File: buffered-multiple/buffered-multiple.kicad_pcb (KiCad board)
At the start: 2 copper layers, 129.5 x 128.5 mm, 67 parts, among them J1 AudioJack_Switch, J10 AudioJack_Switch, J11 Conn_01x06_Pin, J12 Conn_01x06_Socket, J13 AudioJack_Switch, J14 AudioJack_Switch, J15 Conn_02x08_Odd_Even, J16 Conn_01x04_Pin, J17 Conn_01x04_Socket, J2 AudioJack_Switch, J3 AudioJack_Switch, J4 AudioJack_Switch, J5 AudioJack_Switch, J6 AudioJack_Switch, J7 Conn_01x06_Socket, J8 Conn_01x06_Pin, J9 AudioJack_Switch, U1 TL074, U2 TL072, U3 TL074

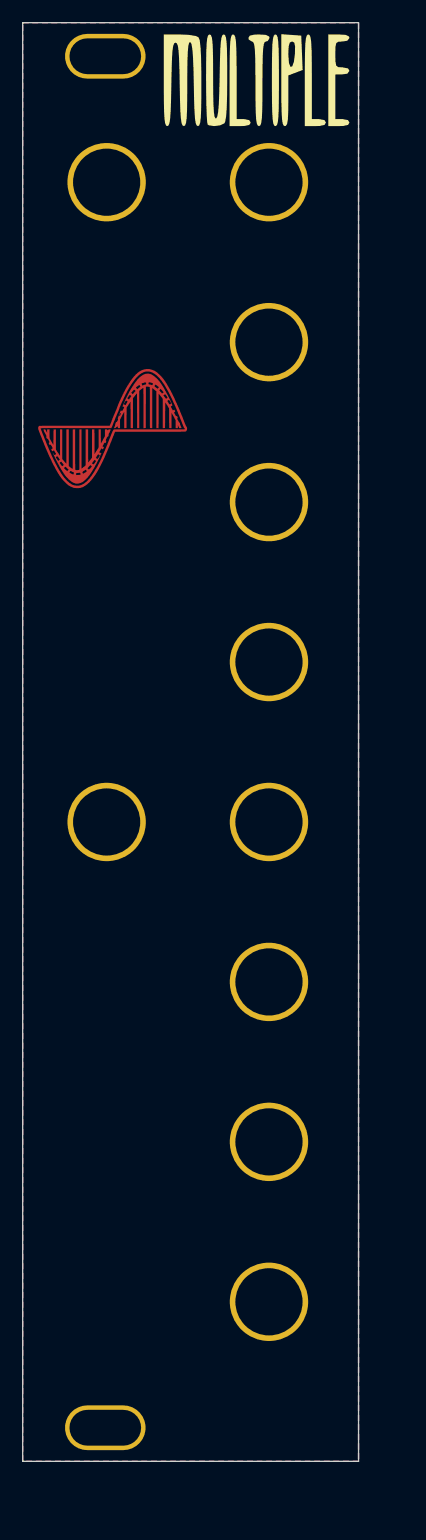
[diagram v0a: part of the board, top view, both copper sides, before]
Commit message: Exponential VCA ver. 1.2
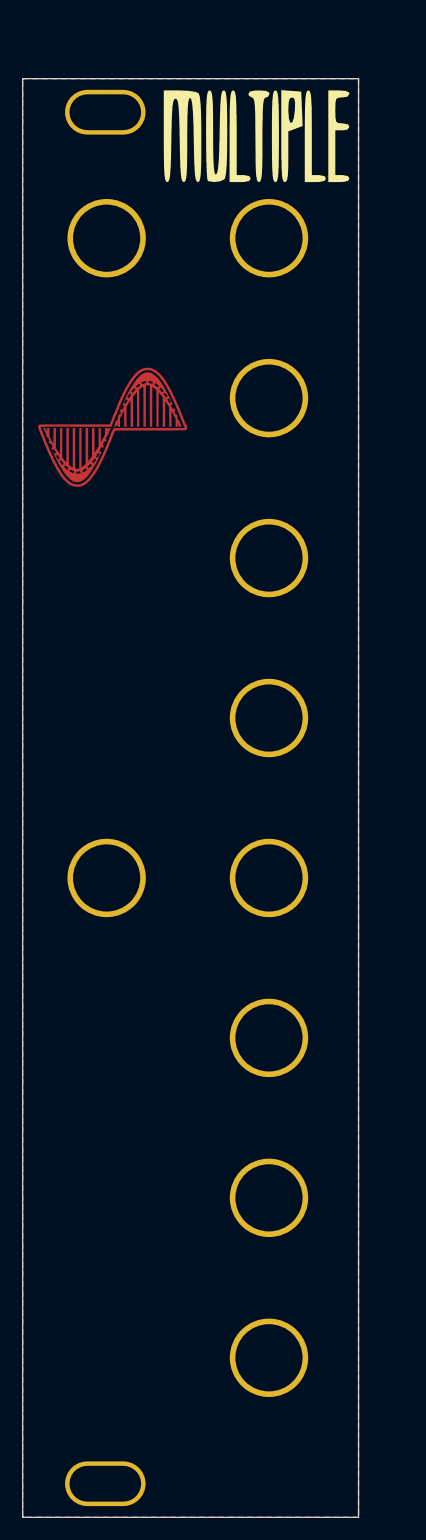
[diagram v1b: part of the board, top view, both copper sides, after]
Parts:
- moved Front 5.00 mm to (39.2, 40.8)
- moved G*** 5.00 mm to (56.0, 46.0)
- moved H3 5.00 mm to (42.5, 55.0)
- moved H8 5.00 mm to (57.0, 55.0)
- moved REF** 5.00 mm to (57.0, 97.9)
- moved REF** 5.00 mm to (42.5, 112.1)
- moved REF** 5.00 mm to (57.0, 126.4)
- moved REF** 5.00 mm to (57.0, 69.3)
- moved REF** 5.00 mm to (50.0, 105.0)
- moved REF** 5.00 mm to (57.0, 155.0)
- moved REF** 5.00 mm to (57.0, 140.7)
- moved REF** 5.00 mm to (57.0, 112.1)
- moved REF** 5.00 mm to (57.0, 83.6)
- moved H1 0.12 mm to (43.0, 71.9)
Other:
- outline, holes or cut-outs redrawn

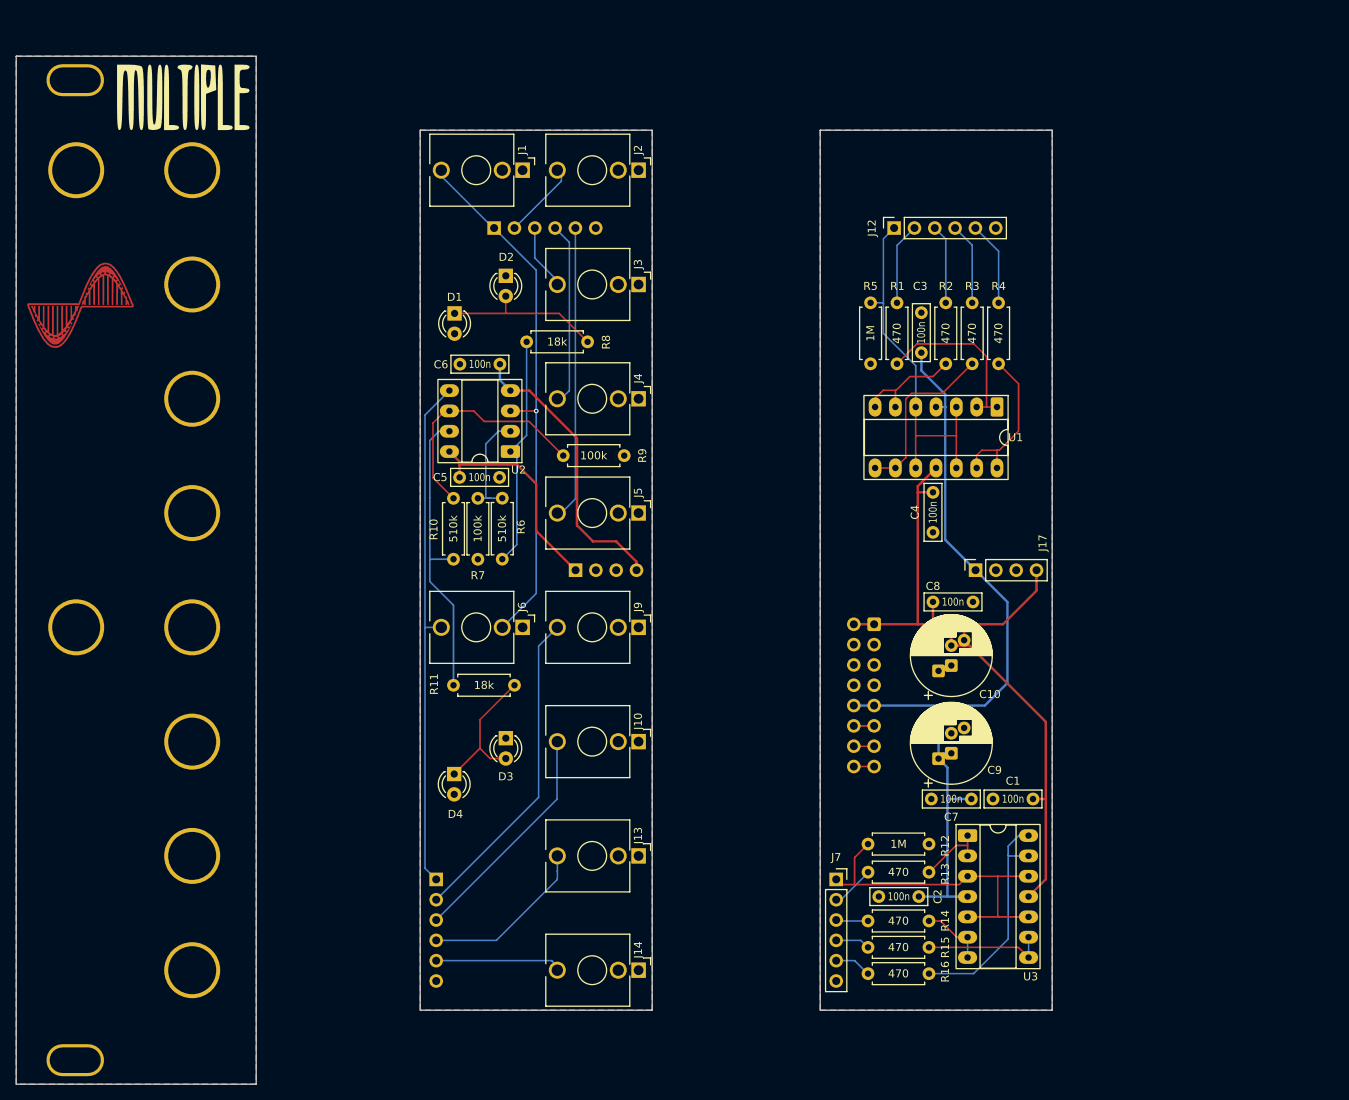
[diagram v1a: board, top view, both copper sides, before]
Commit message: Fixed buffered multiple reversed polarity problem.
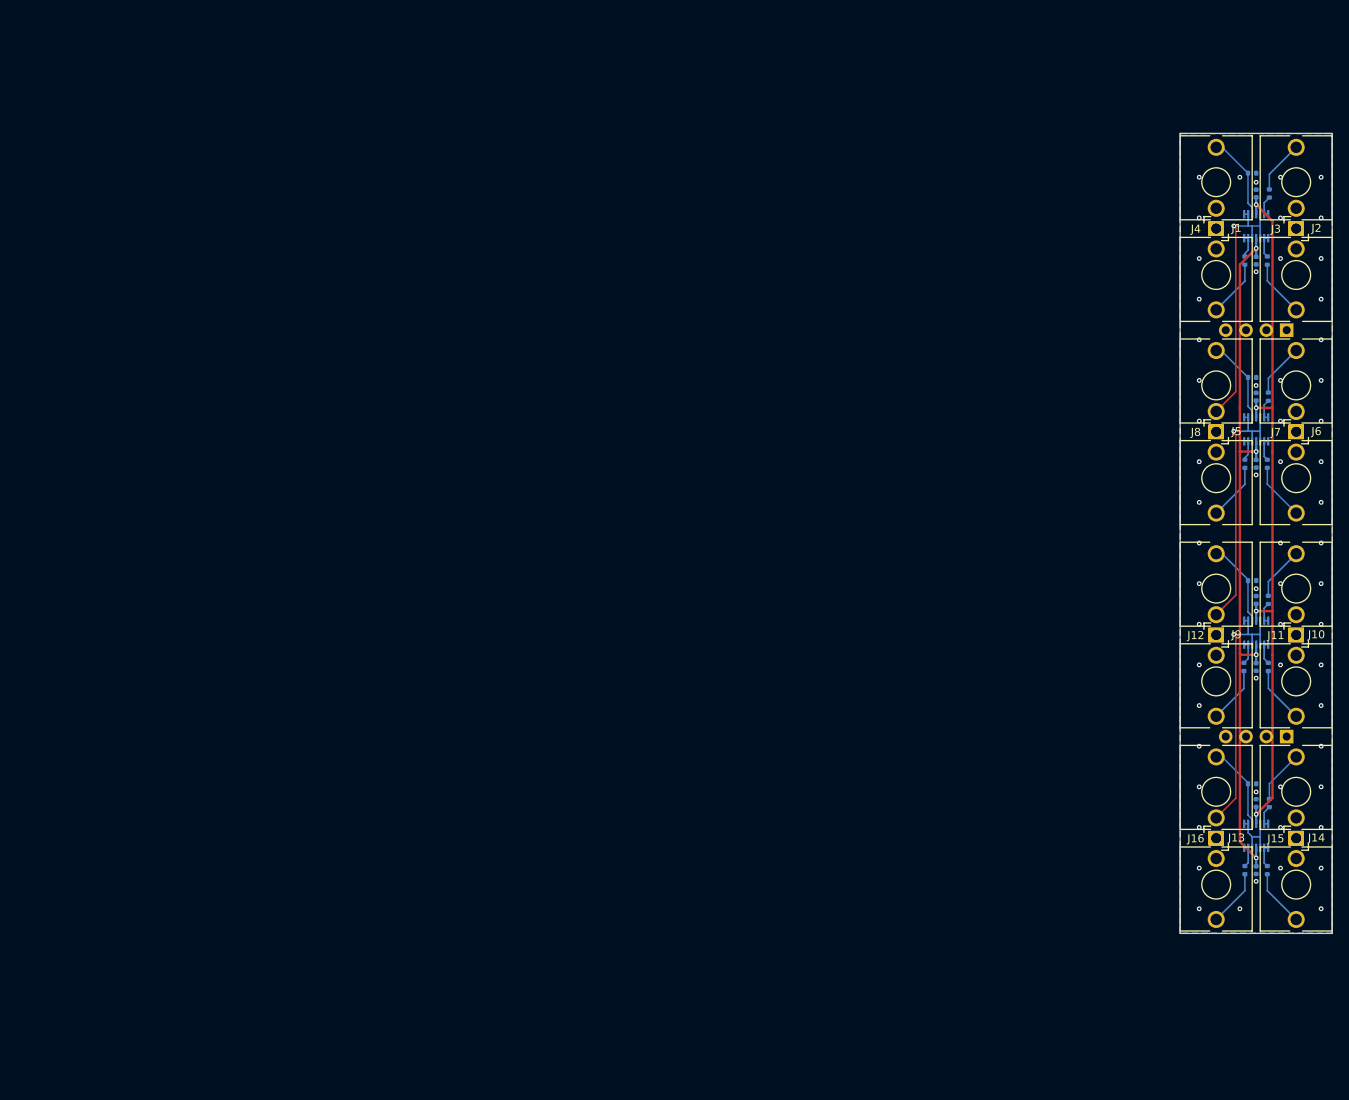
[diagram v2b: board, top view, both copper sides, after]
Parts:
- removed the C1 at (157.1, 133.6)
- removed C10, C9: 47uF, Capacitor_THT:CP_Radial_D10.0mm_P2.50mm_P5.00mm
- removed the C2 at (147.8, 145.8)
- removed Circuit, Front, Jacks: Board, PCM_kikit:Board
- removed D1, D2, D3, D4: LED, LED_THT:LED_D3.0mm
- removed G***: LOGO, LOGO
- removed H1, H2: MountingHole_Pad, 01_Synth_Images:sine-wave-negative
- removed H3, H8: MountingHole_Pad, SynthUX_Components:Panel Jack
- removed the R4 at (157.8, 79.2)
- removed REF** (x8): Panel Jack, SynthUX_Components:Panel Jack
- removed REF**: Eurorack_Panel_3U_6HP, Eurorack_Panel_3U_6HP
- added C3: 100n, Capacitor_SMD:C_0402_1005Metric, B.Cu at (190.0, 83.3)
- added C4: 100n, Capacitor_SMD:C_0402_1005Metric, B.Cu at (190.0, 91.7)
- added J16: AudioJack_Switch, Synth Partd:Jack_3.5mm_Switch, F.Cu at (185.0, 144.3)
- added R5: 1M, Resistor_SMD:R_0402_1005Metric, B.Cu at (189.5, 80.9)
- added U4: TL074, 00_Synth Parts:SOT-23-THIN-14_2x4.2mm_P0.5mm, B.Cu at (190.0, 138.2)
- C1: renamed from C3; footprint Synth Partd:C_Rect_L7.0mm_W2.0mm_P5.00mm -> Capacitor_SMD:C_0402_1005Metric; moved to B.Cu
- C2: renamed from C4; footprint Synth Partd:C_Rect_L7.0mm_W2.0mm_P5.00mm -> Capacitor_SMD:C_0402_1005Metric; moved to B.Cu
- C5, C6, C7, C8: footprint Synth Partd:C_Rect_L7.0mm_W2.0mm_P5.00mm -> Capacitor_SMD:C_0402_1005Metric; moved to B.Cu
- J11, J8: value Conn_01x06_Pin -> AudioJack_Switch; footprint Connector_PinHeader_2.54mm:PinHeader_1x06_P2.54mm_Vertical -> Synth Partd:Jack_3.5mm_Switch; moved to F.Cu
- J12, J7: value Conn_01x06_Socket -> AudioJack_Switch; footprint Connector_PinSocket_2.54mm:PinSocket_1x06_P2.54mm_Vertical -> Synth Partd:Jack_3.5mm_Switch
- J15: value Conn_02x08_Odd_Even -> AudioJack_Switch; footprint Connector_IDC:IDC-Header_2x08_P2.54mm_Vertical -> Synth Partd:Jack_3.5mm_Switch; moved to F.Cu
- J17: value Conn_01x04_Socket -> Conn_01x04_Pin; footprint Connector_PinSocket_2.54mm:PinSocket_1x04_P2.54mm_Vertical -> Connector_PinHeader_2.54mm:PinHeader_1x04_P2.54mm_Vertical; moved to B.Cu
- R1: renamed from R5; footprint Synth Partd:R_Axial_DIN0207_L6.3mm_D2.5mm_P7.62mm_Horizontal -> Resistor_SMD:R_0402_1005Metric; moved to B.Cu
- R10, R6: value 510k -> 470; footprint Synth Partd:R_Axial_DIN0207_L6.3mm_D2.5mm_P7.62mm_Horizontal -> Resistor_SMD:R_0402_1005Metric; moved to B.Cu
- R11, R8: value 18k -> 470; footprint Synth Partd:R_Axial_DIN0207_L6.3mm_D2.5mm_P7.62mm_Horizontal -> Resistor_SMD:R_0402_1005Metric; moved to B.Cu
- R12: value 1M -> 470; footprint Synth Partd:R_Axial_DIN0207_L6.3mm_D2.5mm_P7.62mm_Horizontal -> Resistor_SMD:R_0402_1005Metric; moved to B.Cu
- R13: value 470 -> 1M; footprint Synth Partd:R_Axial_DIN0207_L6.3mm_D2.5mm_P7.62mm_Horizontal -> Resistor_SMD:R_0402_1005Metric; moved to B.Cu
- R14, R15, R16: footprint Synth Partd:R_Axial_DIN0207_L6.3mm_D2.5mm_P7.62mm_Horizontal -> Resistor_SMD:R_0402_1005Metric; moved to B.Cu
- R2: renamed from R1; footprint Synth Partd:R_Axial_DIN0207_L6.3mm_D2.5mm_P7.62mm_Horizontal -> Resistor_SMD:R_0402_1005Metric; moved to B.Cu
- R3: renamed from R2; footprint Synth Partd:R_Axial_DIN0207_L6.3mm_D2.5mm_P7.62mm_Horizontal -> Resistor_SMD:R_0402_1005Metric; moved to B.Cu
- R4: renamed from R3; footprint Synth Partd:R_Axial_DIN0207_L6.3mm_D2.5mm_P7.62mm_Horizontal -> Resistor_SMD:R_0402_1005Metric; moved to B.Cu
- R7: value 100k -> 470; footprint Synth Partd:R_Axial_DIN0207_L6.3mm_D2.5mm_P7.62mm_Horizontal -> Resistor_SMD:R_0402_1005Metric; moved to B.Cu
- R9: value 100k -> 1M; footprint Synth Partd:R_Axial_DIN0207_L6.3mm_D2.5mm_P7.62mm_Horizontal -> Resistor_SMD:R_0402_1005Metric; moved to B.Cu
- U1, U3: footprint Package_DIP:DIP-14_W7.62mm_Socket_LongPads -> 00_Synth Parts:SOT-23-THIN-14_2x4.2mm_P0.5mm; moved to B.Cu
- U2: value TL072 -> TL074; footprint Package_DIP:DIP-8_W7.62mm_Socket_LongPads -> 00_Synth Parts:SOT-23-THIN-14_2x4.2mm_P0.5mm; moved to B.Cu
- moved J11 115.2 mm to (195.0, 118.9), turned to 0 degrees
- moved J8 109.6 mm to (185.0, 93.5), turned to 0 degrees
- moved J6 106.9 mm to (195.0, 81.9), turned to 180 degrees
- moved C6 106.5 mm to (190.0, 117.1), turned to 90 degrees
- moved R10 102.6 mm to (191.5, 108.7), turned to 90 degrees
- moved R11 101.9 mm to (191.5, 117.1), turned to -90 degrees
- moved C5 100.7 mm to (190.0, 108.7), turned to 90 degrees
- moved R7 99.4 mm to (191.4, 91.7), turned to -90 degrees
- moved R6 96.6 mm to (191.5, 83.3), turned to 90 degrees
- moved U2 93.3 mm to (190.0, 87.4), turned to -90 degrees
- moved J1 92.5 mm to (185.0, 56.5), turned to 180 degrees
- moved J18 91.3 mm to (193.8, 125.8), turned to 90 degrees
- moved R8 91.1 mm to (188.6, 91.7), turned to -90 degrees
- moved J14 90.8 mm to (195.0, 132.7), turned to 180 degrees
- moved J10 90.1 mm to (195.0, 107.3), turned to 180 degrees
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- renumbered J16 to J18
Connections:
- C1 pad 1: +12V_2 -> +12V
- C1 pad 2: GND2 -> GND
- C2 pad 1: GND2 -> GND
- C2 pad 2: -12V_2 -> -12V
- C5 pad 1: +12V_1 -> +12V
- C5 pad 2: GND1 -> GND
- C6 pad 1: GND1 -> GND
- C6 pad 2: -12V_1 -> -12V
- C7 pad 1: +12V_2 -> +12V
- C7 pad 2: GND2 -> GND
- C8 pad 1: GND2 -> GND
- C8 pad 2: -12V_2 -> -12V
- J1 pad S: GND1 -> GND
- J1 pad T: IN_1A -> Net-(U1A-+)
- J10 pad S: GND1 -> GND
- J10 pad T: Net-(J8-Pin_3) -> Net-(J10-PadT)
- J13 pad S: GND1 -> GND
- J13 pad T: Net-(J8-Pin_4) -> Net-(U4A-+)
- J13 pad TN: unconnected-(J13-PadTN) -> Net-(U3A--)
- J14 pad S: GND1 -> GND
- J14 pad T: Net-(J8-Pin_5) -> Net-(J14-PadT)
- J17 pad 1: +12V_2 -> GND
- J17 pad 2: GND2 -> +12V
- J17 pad 3: GND2 -> -12V
- J17 pad 4: -12V_2 -> GND
- J18 pad 1: +12V_1 -> GND
- J18 pad 2: GND1 -> +12V
- J18 pad 3: GND1 -> -12V
- J18 pad 4: -12V_1 -> GND
- J2 pad S: GND1 -> GND
- J2 pad T: Net-(J11-Pin_2) -> Net-(J2-PadT)
- J3 pad S: GND1 -> GND
- J3 pad T: Net-(J11-Pin_3) -> Net-(J3-PadT)
- J4 pad S: GND1 -> GND
- J4 pad T: Net-(J11-Pin_4) -> Net-(J4-PadT)
- J5 pad S: GND1 -> GND
- J5 pad T: Net-(J11-Pin_5) -> Net-(U2A-+)
- J5 pad TN: unconnected-(J5-PadTN) -> Net-(U1A--)
- J6 pad S: GND1 -> GND
- J6 pad T: IN_1B -> Net-(J6-PadT)
- J6 pad TN: IN_1A -> unconnected-(J6-PadTN)
- J9 pad S: GND1 -> GND
- J9 pad T: Net-(J8-Pin_2) -> Net-(U3A-+)
- J9 pad TN: unconnected-(J9-PadTN) -> NORMED
- R1 pad 1: GND2 -> GND
- R1 pad 2: IN_2A -> Net-(U1A-+)
- R10 pad 1: Net-(U2B--) -> Net-(U3B--)
- R10 pad 2: Net-(R10-Pad2) -> Net-(J10-PadT)
- R11 pad 1: Net-(R10-Pad2) -> Net-(U3C--)
- R11 pad 2: Net-(D3-A) -> Net-(J11-PadT)
- R12 pad 1: GND2 -> Net-(U3D--)
- R12 pad 2: IN_2B -> Net-(J12-PadT)
- R13 pad 1: Net-(U3A--) -> GND
- R13 pad 2: Net-(J7-Pin_2) -> Net-(U4A-+)
- R14 pad 1: Net-(U3B--) -> Net-(U4B--)
- R14 pad 2: Net-(J7-Pin_3) -> Net-(J14-PadT)
- R15 pad 1: Net-(U3C--) -> Net-(U4C--)
- R15 pad 2: Net-(J7-Pin_4) -> Net-(J15-PadT)
- R16 pad 1: Net-(U3D--) -> Net-(U4D--)
- R16 pad 2: Net-(J7-Pin_5) -> Net-(J16-PadT)
- R2 pad 1: Net-(U1A--) -> Net-(U1B--)
- R2 pad 2: Net-(J12-Pin_2) -> Net-(J2-PadT)
- R3 pad 1: Net-(U1B--) -> Net-(U1C--)
- R3 pad 2: Net-(J12-Pin_3) -> Net-(J3-PadT)
- R4 pad 1: Net-(U1C--) -> Net-(U1D--)
- R4 pad 2: Net-(J12-Pin_4) -> Net-(J4-PadT)
- R6 pad 1: Net-(U2A--) -> Net-(U2B--)
- R6 pad 2: Net-(R6-Pad2) -> Net-(J6-PadT)
- R7 pad 1: GND1 -> Net-(U2C--)
- R7 pad 2: Net-(U2A--) -> Net-(J7-PadT)
- R8 pad 1: Net-(R6-Pad2) -> Net-(U2D--)
- R8 pad 2: Net-(D1-K) -> Net-(J8-PadT)
- R9 pad 1: GND1 -> GND
- R9 pad 2: Net-(U2B--) -> Net-(U3A-+)
- U1 pad 10: IN_2A -> Net-(U1A--)
- U1 pad 11: -12V_2 -> -12V
- U1 pad 12: IN_2A -> Net-(U1A--)
- U1 pad 3: IN_2A -> Net-(U1A-+)
- U1 pad 4: +12V_2 -> +12V
- U1 pad 5: IN_2A -> Net-(U1A--)
- U2 pad 1: Net-(R6-Pad2) -> NORMED
- U2 pad 2: Net-(U2A--) -> NORMED
- U2 pad 3: IN_1A -> Net-(U2A-+)
- U2 pad 4: -12V_1 -> +12V
- U2 pad 5: IN_1B -> NORMED
- U2 pad 7: Net-(R10-Pad2) -> Net-(U2B--)
- U2 pad 8: +12V_1 -> Net-(U2C--)
- U3 pad 10: IN_2B -> Net-(U3A--)
- U3 pad 11: -12V_2 -> -12V
- U3 pad 12: IN_2B -> Net-(U3A--)
- U3 pad 3: IN_2B -> Net-(U3A-+)
- U3 pad 4: +12V_2 -> +12V
- U3 pad 5: IN_2B -> Net-(U3A--)
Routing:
- net +12V_2: track 102.6 -> 0.00 mm
- net -12V_2: track 97.0 -> 0.00 mm
- net -12V: track 0.00 -> 91.3 mm, vias 0 -> 4
- net +12V: track 0.00 -> 91.2 mm, vias 0 -> 4
- net IN_1A: track 67.1 -> 0.00 mm, vias 1 -> 0
- net IN_1B: track 65.0 -> 0.00 mm
- net IN_2A: track 46.5 -> 0.00 mm
- net IN_2B: track 43.2 -> 0.00 mm
- net Net-(J8-Pin_2): track 40.3 -> 0.00 mm
- net Net-(R10-Pad2): track 37.7 -> 0.00 mm
- net Net-(J11-Pin_5): track 36.4 -> 0.00 mm
- net -12V_1: track 35.9 -> 0.00 mm
- net NORMED: track 0.00 -> 33.9 mm, vias 0 -> 1
- net Net-(R6-Pad2): track 29.1 -> 0.00 mm
- net Net-(J8-Pin_3): track 28.8 -> 0.00 mm
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- added copper zone on B.Cu, net GND
- added copper zone on F.Cu, net GND
- removed copper zone on B.Cu, net (none)
- removed copper zone on F.Cu, net (none)
- removed copper zone on B.Cu, net GND1
- removed copper zone on F.Cu, net GND1
- removed copper zone on B.Cu, net GND2
- removed copper zone on F.Cu, net GND2
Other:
- board size 129.5 x 128.5 mm -> 19 x 100 mm
- board text added: "Buffered Multi v2.1 5/2026"
- board text added: "GND +12V -12V GND"
- board text added: "JLCJLCJLCJLC"
- board text removed: "Eurorack_Panel_3U_6HP"
